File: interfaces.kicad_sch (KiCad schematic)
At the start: 0 parts

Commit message: Modify project's Title Block
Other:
- company: (none) -> Antmicro Ltd
- title: Jetson Orin Baseboard -> Jetson Orin NX Baseboard
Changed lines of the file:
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@@
   (paper "A3")
   (title_block
-    (title "Jetson Orin Baseboard")
+    (title "Jetson Orin NX Baseboard")
+    (company "Antmicro Ltd")
     (comment 1 "www.antmicro.com")
-    (comment 2 "Antmicro Ltd")
   )
   (image (at 76.2 275.59) (scale 0.15)

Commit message: Add USB2.0 HUB, place passives to USB, add mockup connections to SOM and USB
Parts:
- added J8: Raspberry_Pi_2_3, symbol Connector:Raspberry_Pi_2_3
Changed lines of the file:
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@@
     )
   )
+  (symbol (lib_id "Connector:Raspberry_Pi_2_3") (at 314.325 147.955 0) (unit 1)
+    (in_bom yes) (on_board yes) (fields_autoplaced)
+    (property "Reference" "J8" (id 0) (at 321.4244 113.7752 0)
+      (effects (font (size 1.27 1.27)) (justify left))
+    )
+    (property "Value" "Raspberry_Pi_2_3" (id 1) (at 321.4244 116.3121 0)
+      (effects (font (size 1.27 1.27)) (justify left))
+    )
+    (property "Footprint" "" (id 2) (at 314.325 147.955 0)
+      (effects (font (size 1.27 1.27)) hide)
+    )
+    (property "Datasheet" "https://www.raspberrypi.org/documentation/hardware/raspberrypi/schematics/rpi_SCH_3bplus_1p0_reduced.pdf" (id 3) (at 314.325 147.955 0)
+      (effects (font (size 1.27 1.27)) hide)
+    )
+    (pin "1")
+    (pin "10")
+    (pin "11")
+    (pin "12")
+    (pin "13")
+    (pin "14")
+    (pin "15")
+    (pin "16")
+    (pin "17")
+    (pin "18")
+    (pin "19")
+    (pin "2")
+    (pin "20")
+    (pin "21")
+    (pin "22")
+    (pin "23")
+    (pin "24")
+    (pin "25")
+    (pin "26")
+    (pin "27")
+    (pin "28")
+    (pin "29")
+    (pin "3")
+    (pin "30")
+    (pin "31")
+    (pin "32")
+    (pin "33")
+    (pin "34")
+    (pin "35")
+    (pin "36")
+    (pin "37")
+    (pin "38")
+    (pin "39")
+    (pin "4")
+    (pin "40")
+    (pin "5")
+    (pin "6")
+    (pin "7")
+    (pin "8")
+    (pin "9")
+  )
 )

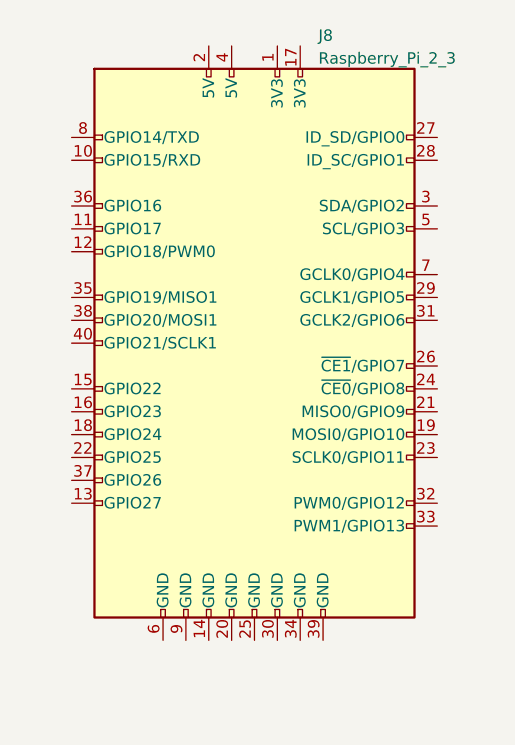
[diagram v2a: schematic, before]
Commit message: Added ESD protection for USB connectors
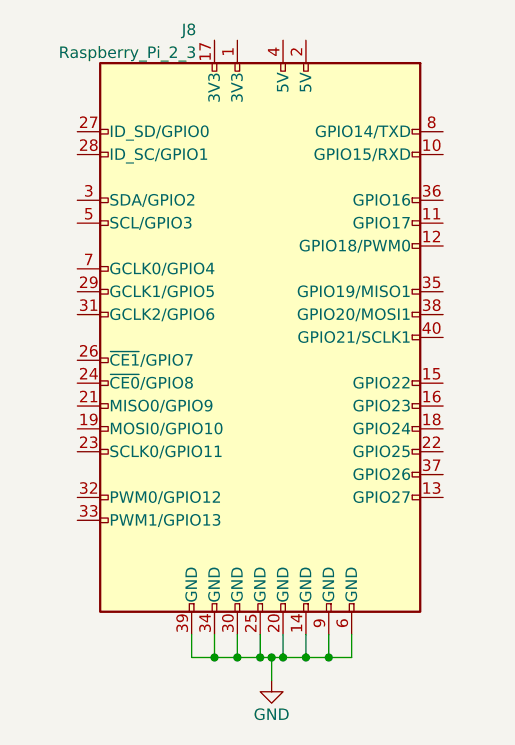
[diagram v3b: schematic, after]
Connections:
- net GND: now reaches J8.14 (GND)
- net GND: now also J8.20 (GND), J8.25 (GND), J8.30 (GND), J8.34 (GND), J8.39 (GND), J8.6 (GND), J8.9 (GND)
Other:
- moved on the sheet: J8
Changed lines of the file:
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@@
     (comment 1 "www.antmicro.com")
+  )
+  (junction (at 320.04 182.88) (diameter 0) (color 0 0 0 0)
+  )
+  (junction (at 322.58 182.88) (diameter 0) (color 0 0 0 0)
+  )
+  (junction (at 309.88 182.88) (diameter 0) (color 0 0 0 0)
+  )
+  (junction (at 317.5 182.88) (diameter 0) (color 0 0 0 0)
+  )
+  (junction (at 316.23 182.88) (diameter 0) (color 0 0 0 0)
+  )
+  (junction (at 314.96 182.88) (diameter 0) (color 0 0 0 0)
+  )
+  (junction (at 312.42 182.88) (diameter 0) (color 0 0 0 0)
+  )
+  (wire (pts (xy 307.34 182.88) (xy 307.34 180.34))
+    (stroke (width 0) (type default) (color 0 0 0 0))
+  )
+  (wire (pts (xy 322.58 180.34) (xy 322.58 182.88))
+    (stroke (width 0) (type default) (color 0 0 0 0))
+  )
+  (wire (pts (xy 312.42 182.88) (xy 309.88 182.88))
+    (stroke (width 0) (type default) (color 0 0 0 0))
+  )
+  (wire (pts (xy 316.23 182.88) (xy 314.96 182.88))
+    (stroke (width 0) (type default) (color 0 0 0 0))
+  )
+  (wire (pts (xy 309.88 180.34) (xy 309.88 182.88))
+    (stroke (width 0) (type default) (color 0 0 0 0))
+  )
+  (wire (pts (xy 314.96 182.88) (xy 312.42 182.88))
+    (stroke (width 0) (type default) (color 0 0 0 0))
+  )
+  (wire (pts (xy 325.12 180.34) (xy 325.12 182.88))
+    (stroke (width 0) (type default) (color 0 0 0 0))
+  )
+  (wire (pts (xy 320.04 180.34) (xy 320.04 182.88))
+    (stroke (width 0) (type default) (color 0 0 0 0))
+  )
+  (wire (pts (xy 322.58 182.88) (xy 320.04 182.88))
+    (stroke (width 0) (type default) (color 0 0 0 0))
+  )
+  (wire (pts (xy 314.96 180.34) (xy 314.96 182.88))
+    (stroke (width 0) (type default) (color 0 0 0 0))
+  )
+  (wire (pts (xy 316.23 182.88) (xy 316.23 185.42))
+    (stroke (width 0) (type default) (color 0 0 0 0))
+  )
+  (wire (pts (xy 317.5 180.34) (xy 317.5 182.88))
+    (stroke (width 0) (type default) (color 0 0 0 0))
+  )
+  (wire (pts (xy 317.5 182.88) (xy 316.23 182.88))
+    (stroke (width 0) (type default) (color 0 0 0 0))
+  )
+  (wire (pts (xy 320.04 182.88) (xy 317.5 182.88))
+    (stroke (width 0) (type default) (color 0 0 0 0))
+  )
+  (wire (pts (xy 312.42 180.34) (xy 312.42 182.88))
+    (stroke (width 0) (type default) (color 0 0 0 0))
+  )
+  (wire (pts (xy 325.12 182.88) (xy 322.58 182.88))
+    (stroke (width 0) (type default) (color 0 0 0 0))
+  )
+  (wire (pts (xy 309.88 182.88) (xy 307.34 182.88))
+    (stroke (width 0) (type default) (color 0 0 0 0))
   )
   (image (at 76.2 275.59) (scale 0.15)
@@
     )
   )
-  (symbol (lib_id "Connector:Raspberry_Pi_2_3") (at 314.325 147.955 0) (unit 1)
+  (symbol (lib_id "power:GND") (at 316.23 185.42 0) (mirror y) (unit 1)
+    (in_bom yes) (on_board yes)
+    (property "Reference" "#PWR?" (id 0) (at 316.23 191.77 0)
+      (effects (font (size 1.27 1.27)) hide)
+    )
+    (property "Value" "GND" (id 1) (at 316.23 189.23 0))
+    (property "Footprint" "" (id 2) (at 316.23 185.42 0)
+      (effects (font (size 1.27 1.27)) hide)
+    )
+    (property "Datasheet" "" (id 3) (at 316.23 185.42 0)
+      (effects (font (size 1.27 1.27)) hide)
+    )
+    (pin "1")
+  )
+  (symbol (lib_id "Connector:Raspberry_Pi_2_3") (at 314.96 147.32 0) (mirror y) (unit 1)
     (in_bom yes) (on_board yes) (fields_autoplaced)
-    (property "Reference" "J8" (id 0) (at 321.4244 113.7752 0)
+    (property "Reference" "J8" (id 0) (at 307.8606 113.1402 0)
       (effects (font (size 1.27 1.27)) (justify left))
     )
-    (property "Value" "Raspberry_Pi_2_3" (id 1) (at 321.4244 116.3121 0)
+    (property "Value" "Raspberry_Pi_2_3" (id 1) (at 307.8606 115.6771 0)
       (effects (font (size 1.27 1.27)) (justify left))
     )
-    (property "Footprint" "" (id 2) (at 314.325 147.955 0)
+    (property "Footprint" "" (id 2) (at 314.96 147.32 0)
       (effects (font (size 1.27 1.27)) hide)
     )
-    (property "Datasheet" "https://www.raspberrypi.org/documentation/hardware/raspberrypi/schematics/rpi_SCH_3bplus_1p0_reduced.pdf" (id 3) (at 314.325 147.955 0)
+    (property "Datasheet" "https://www.raspberrypi.org/documentation/hardware/raspberrypi/schematics/rpi_SCH_3bplus_1p0_reduced.pdf" (id 3) (at 314.96 147.32 0)
       (effects (font (size 1.27 1.27)) hide)
     )
